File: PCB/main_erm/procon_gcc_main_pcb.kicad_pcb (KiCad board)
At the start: 4 copper layers, 110.9 x 59.7 mm, 130 parts, among them J1 Conn_01x04_Pin, J3 To Button Board, J5 Conn_01x02_Pin, J9 USB_C_Receptacle, Q1 Q_PMOS_GDS, Q2 Q_NMOS_GSD, Q3 Q_NMOS_GSD, Q4 BSS138DW, Q5 BSS138DW, Q7 MMBT3904, Q8 MMBT3904, SW1 GL18_SW, SW2 GL18_SW, SW3 1TS026A-1000-0550, SW4 TS35CA, SW5 1TS026A-1000-0550, T1 36-8730, T2 36-8730, T3 36-8730, T4 36-8730, U1 GH39F (Hall SOT23), U10 MCP3002, U11 ST_LSM6, U12 PI3USB4000A, U13 GD25Q80EEIGR, U14 TPS630001RCR, U16 BQ25180, U2 GH39F (Hall SOT23), U3 GH39F (Hall SOT23), U4 GH39F (Hall SOT23), U5 ST_LSM6, U6 RP2040, U7 CH340K, U8 MCP3002, U9 ESP32-PICO-MINI-02, Y1 Crystal_GND3

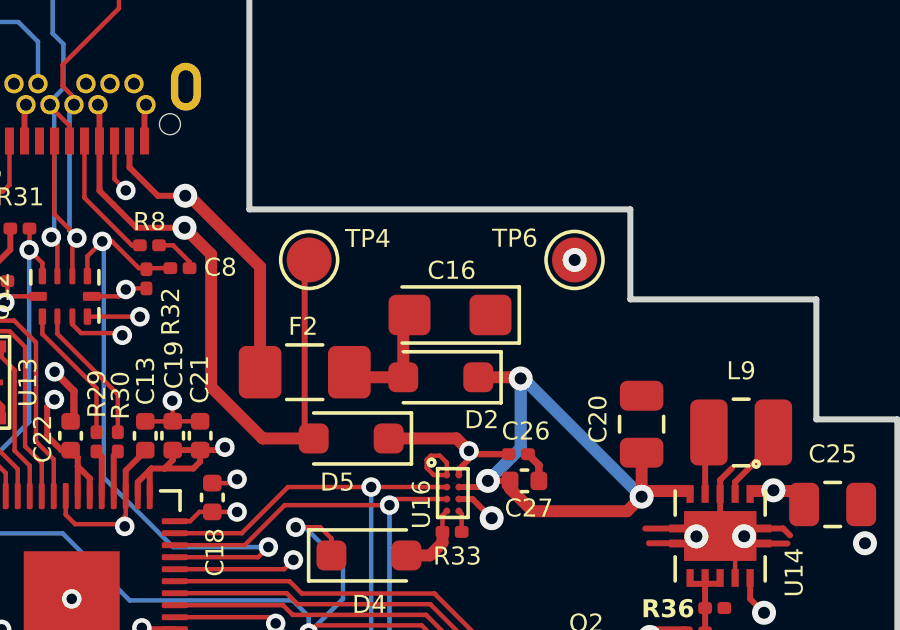
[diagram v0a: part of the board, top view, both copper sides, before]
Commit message: PCB and FW Updates
- Add player number support internally
- Add debug for bt baseband updating
- Orange indication for baseband update mode
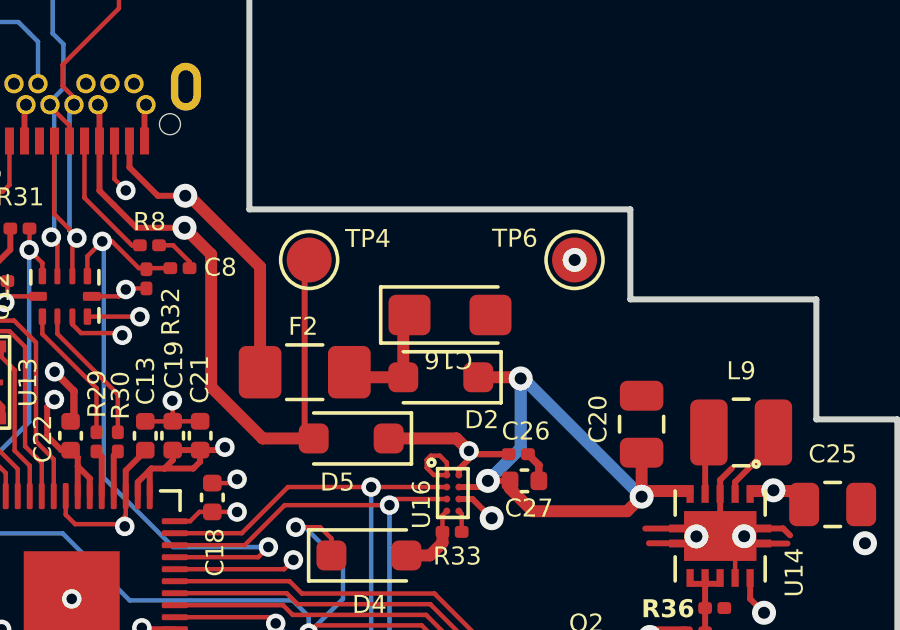
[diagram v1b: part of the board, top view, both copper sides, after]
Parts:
- turned C16 to 0 degrees
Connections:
- C16 pad 1: GND -> Net-(D2-A)
- C16 pad 2: Net-(D2-A) -> GND
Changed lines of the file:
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@@
   )
   (footprint "Capacitor_Tantalum_SMD:CP_EIA-3216-18_Kemet-A" (layer "F.Cu")
-    (at 151.394334 104.63454 180)
+    (at 151.394334 104.63454)
     (descr "Tantalum Capacitor SMD Kemet-A (3216-18 Metric), IPC_7351 nominal, (Body size from: http://www.kemet.com/Lists/ProductCatalog/Attachments/253/KEM_TC101_STD.pdf), generated with kicad-footprint-generator")
     (tags "capacitor tantalum")
@@
     (property "ki_keywords" "cap capacitor")
     (attr smd)
-    (fp_text reference "C16" (at -0.055666 1.48454 unlocked) (layer "F.SilkS")
+    (fp_text reference "C16" (at -0.055666 1.48454 -180 unlocked) (layer "F.SilkS")
         (effects (font (size 0.6 0.6) (thickness 0.1)))
     )
@@
     (fp_line (start 1.6 0.8) (end 1.6 -0.8)
       (stroke (width 0.1) (type solid)) (layer "F.Fab"))
-    (pad "1" smd roundrect (at -1.35 0 180) (size 1.4 1.35) (layers "F.Cu" "F.Paste" "F.Mask") (roundrect_rratio 0.1851851852)
+    (pad "1" smd roundrect (at -1.35 0) (size 1.4 1.35) (layers "F.Cu" "F.Paste" "F.Mask") (roundrect_rratio 0.1851851852)
+      (net 136 "Net-(D2-A)") (pintype "passive"))
+    (pad "2" smd roundrect (at 1.35 0) (size 1.4 1.35) (layers "F.Cu" "F.Paste" "F.Mask") (roundrect_rratio 0.1851851852)
       (net 2 "GND") (pintype "passive"))
-    (pad "2" smd roundrect (at 1.35 0 180) (size 1.4 1.35) (layers "F.Cu" "F.Paste" "F.Mask") (roundrect_rratio 0.1851851852)
-      (net 136 "Net-(D2-A)") (pintype "passive"))
     (model "${KICAD6_3DMODEL_DIR}/Capacitor_Tantalum_SMD.3dshapes/CP_EIA-3216-18_Kemet-A.wrl"
       (offset (xyz 0 0 0))
